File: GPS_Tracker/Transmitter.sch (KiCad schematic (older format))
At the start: 4 parts

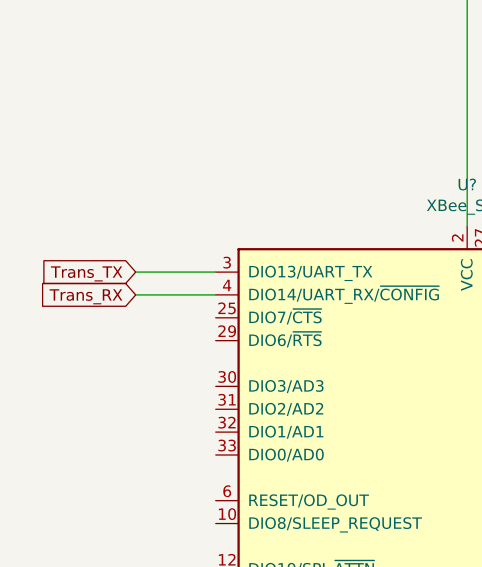
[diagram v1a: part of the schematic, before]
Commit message: added hichary labels
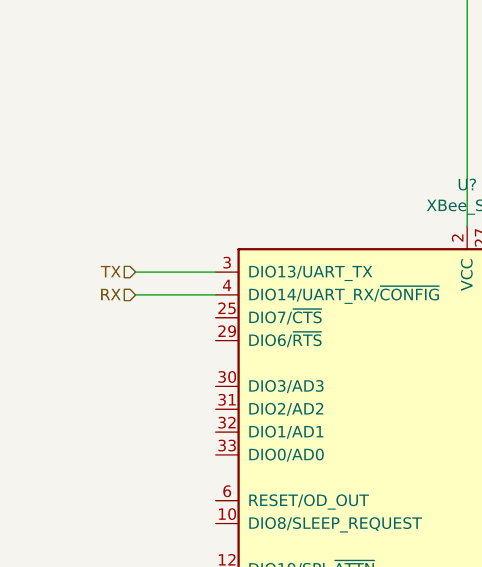
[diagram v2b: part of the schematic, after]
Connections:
- net Trans_RX renamed RX
- net Trans_TX renamed TX
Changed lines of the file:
@@
 Wire Wire Line
 	5150 2050 5150 3250
-Text GLabel 3700 3450 0    50   Input ~ 0
-Trans_TX
-Text GLabel 3700 3550 0    50   Input ~ 0
-Trans_RX
 Wire Wire Line
 	4050 3450 3700 3450
 Wire Wire Line
 	4050 3550 3700 3550
+Text HLabel 3700 3450 0    50   Input ~ 0
+TX
+Text HLabel 3700 3550 0    50   Input ~ 0
+RX
 $EndSCHEMATC
